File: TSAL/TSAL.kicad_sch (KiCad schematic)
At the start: 57 parts, among them J1 Conn_02x03_Counter_Clockwise, J2 Conn_01x02, J3 Conn_02x01, J4 Conn_02x01, Q1 BSS138, Q2 BSS138, Q3 AO3401A, U1 LM358, U10 74HC74, U2 74HC27, U3 74HC20, U4 4N35, U5 74HC08, U6 74HC86, U7 LM7805_TO220, U8 LM339, U9 LM339

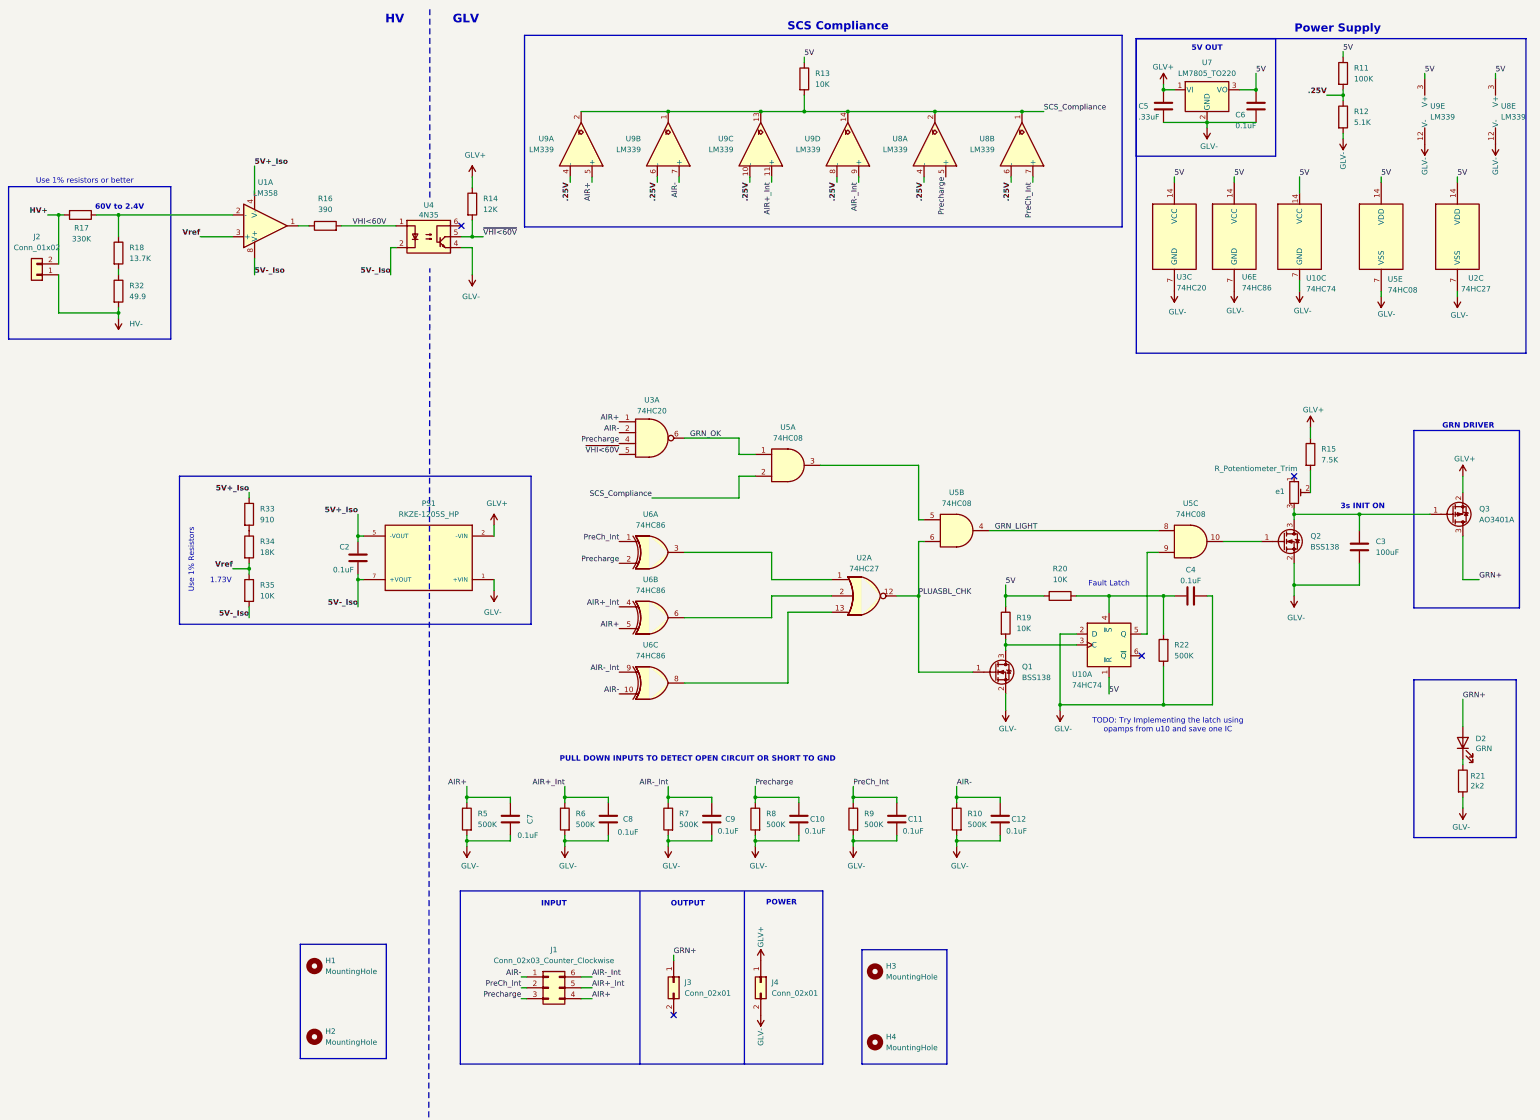
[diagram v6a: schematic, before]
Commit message: added hierarchichal labels for hierarchical sheet compatibility
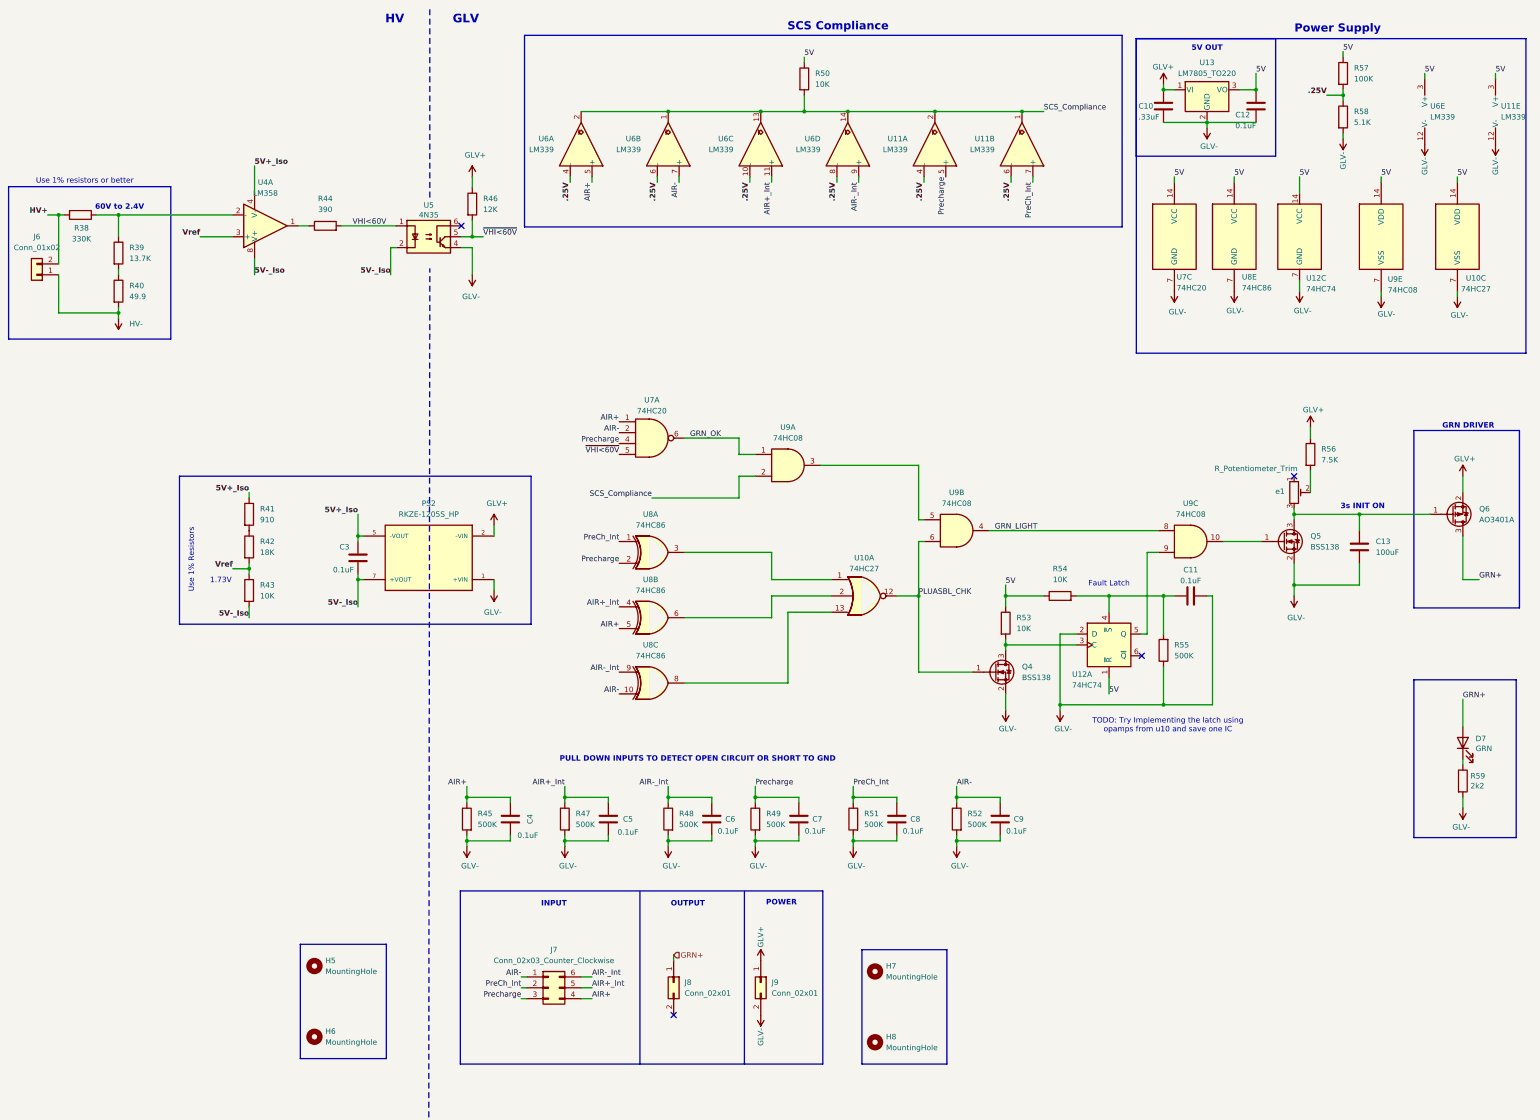
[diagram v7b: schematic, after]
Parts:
- renumbered C5 to C10, C4 to C11, C6 to C12, C3 to C13, C2 to C3, C7 to C4, C8 to C5, C9 to C6, C10 to C7, C11 to C8, C12 to C9, D2 to D7, H1 to H5, H2 to H6, H3 to H7, H4 to H8, J2 to J6, J1 to J7, J3 to J8, J4 to J9, PS1 to PS2, Q1 to Q4, Q2 to Q5, Q3 to Q6, R17 to R38, R18 to R39, R32 to R40, R33 to R41, R34 to R42, R35 to R43, R16 to R44, R5 to R45, R14 to R46, R6 to R47, R7 to R48, R8 to R49, R13 to R50, R9 to R51, R10 to R52, R19 to R53, R20 to R54, R22 to R55, R15 to R56, R11 to R57, R12 to R58, R21 to R59, U2 to U10, U8 to U11, U10 to U12, U7 to U13, U1 to U4, U4 to U5, U9 to U6, U3 to U7, U6 to U8, U5 to U9
